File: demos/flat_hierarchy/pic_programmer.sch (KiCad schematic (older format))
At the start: 50 parts, among them J1 DB9-FEMAL, P1 CONN_2, Q1 BC237, Q2 BC307, Q3 BC307, U2 74HC125, U3 7805, U4 LT1373

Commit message: Update demo files
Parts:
- D12: Champ4 (none) -> YELLOW-LED
- D8: Champ4 (none) -> Low Current Led; Champ5 (none) -> RED LED
- D9: Champ4 (none) -> GREEN LED
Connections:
- net VPP/MCLR renamed VPP-MCLR

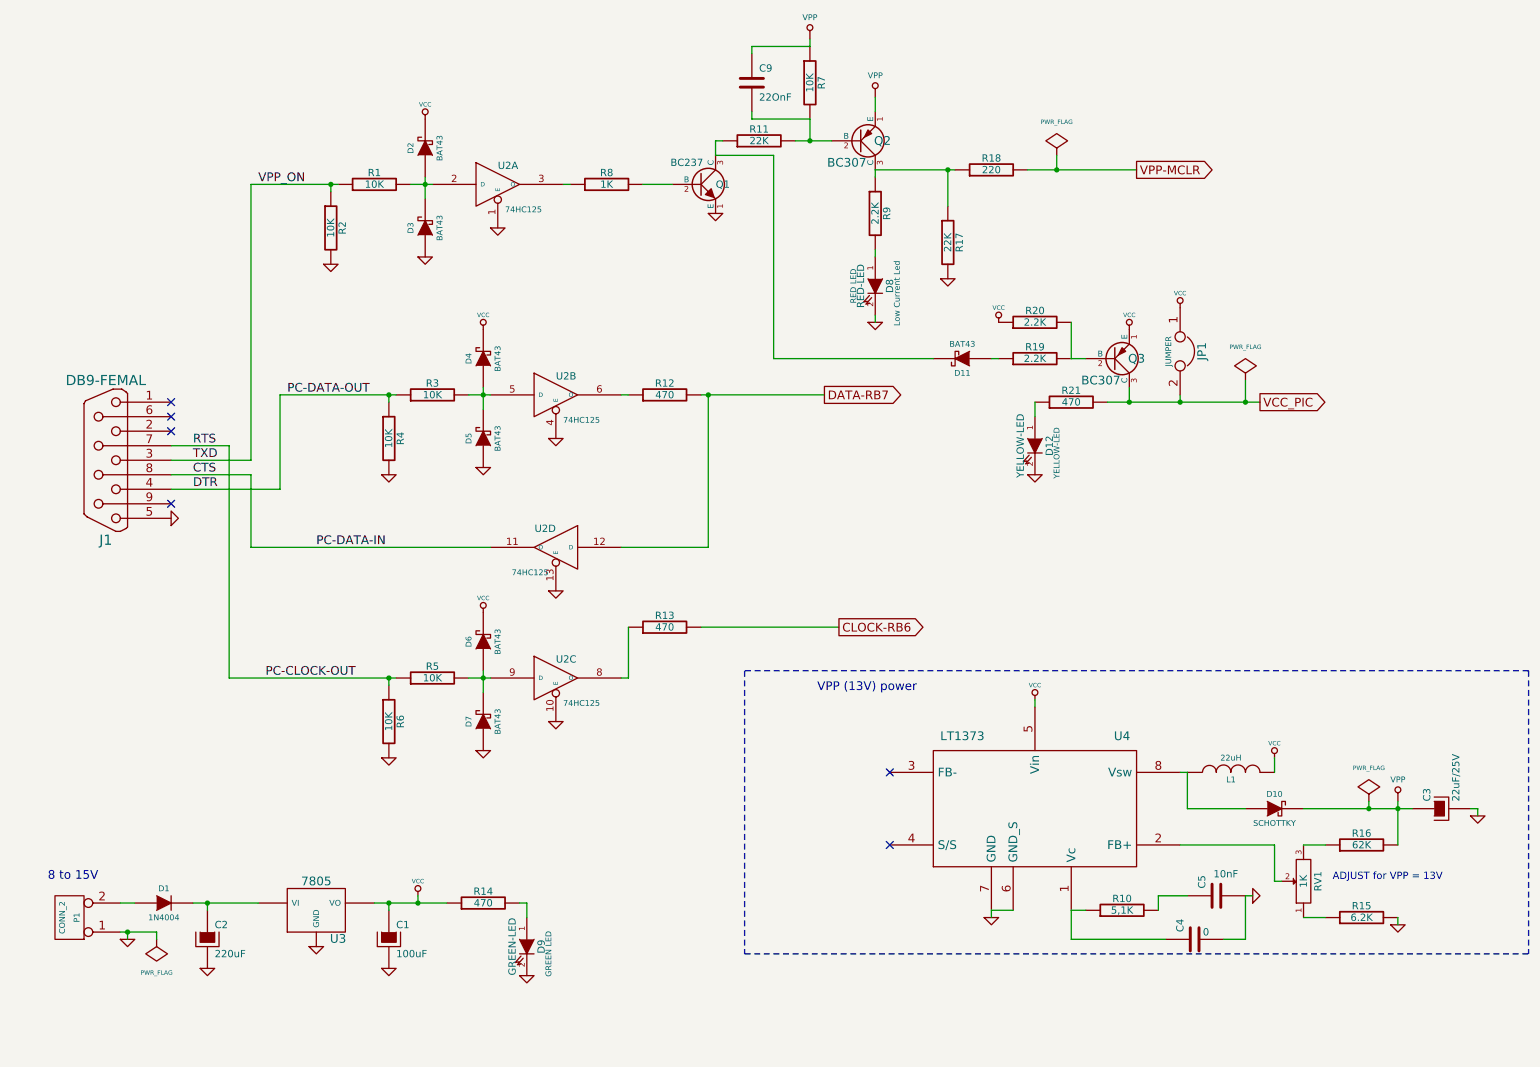
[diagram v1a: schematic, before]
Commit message: demos/ schematic tidying
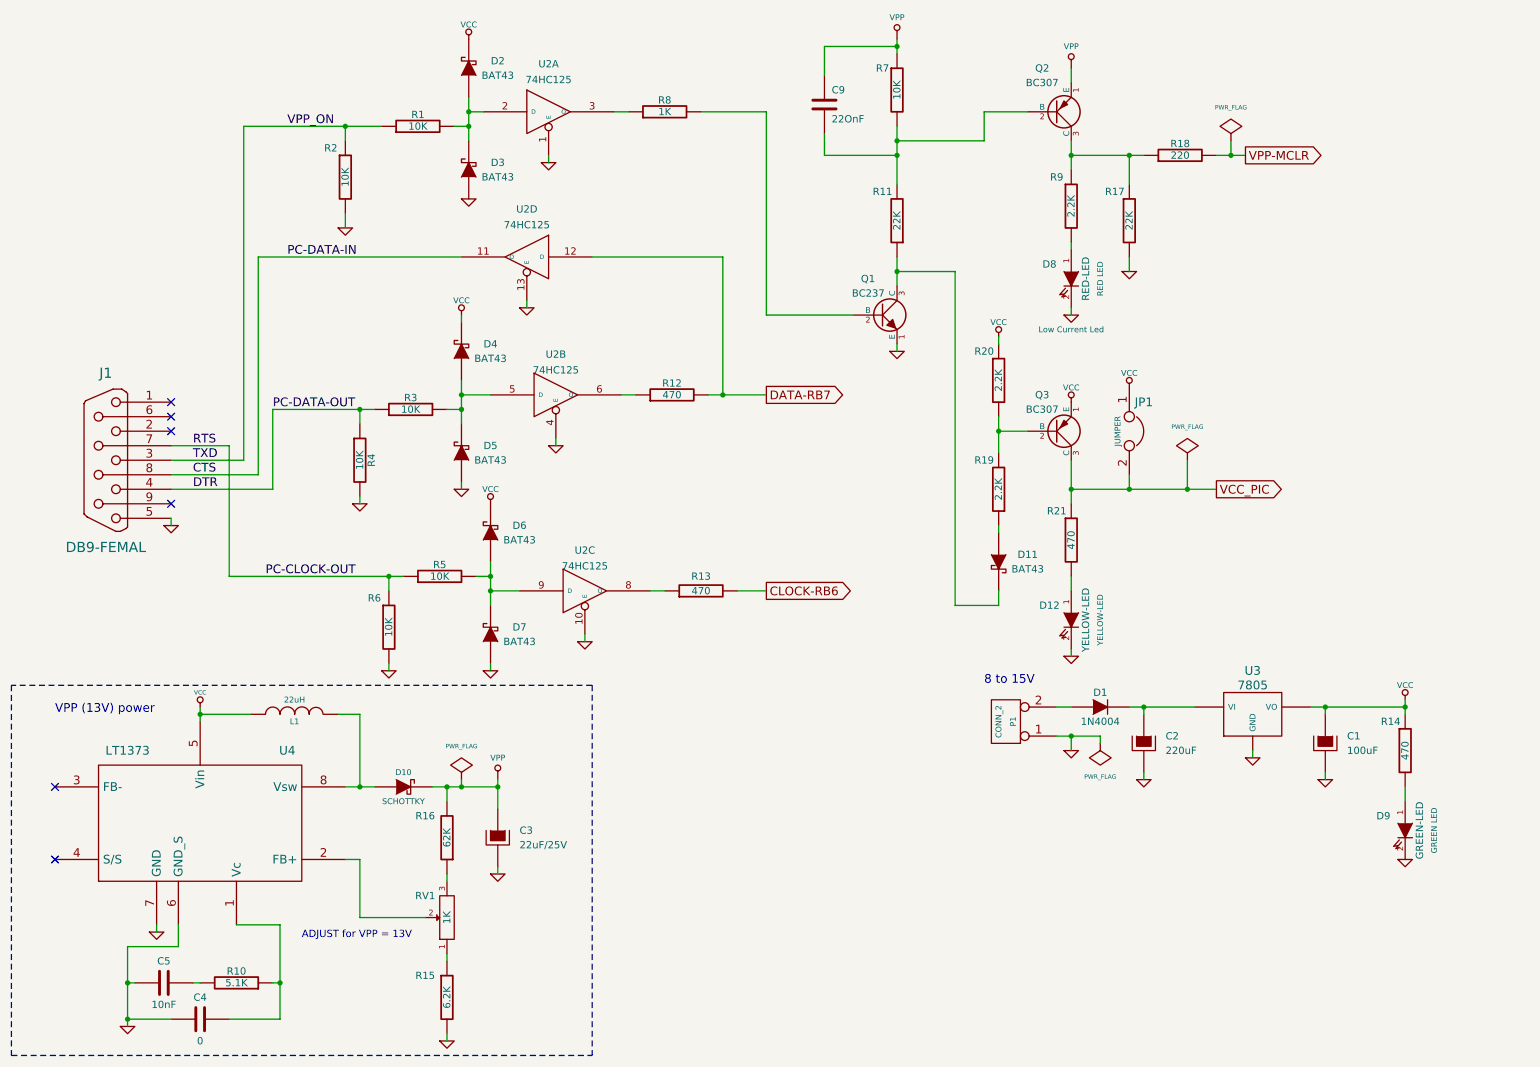
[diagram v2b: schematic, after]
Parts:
- R10: value 5,1K -> 5.1K
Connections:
- net VCC_PIC: now also R21.1; no longer R21.2
- net at D12.1 (A): now also R21.2; no longer R21.1
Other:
- moved on the sheet: C1, C2, C3, C4, C5, C9, D1, D10, D11, D12, D2, D3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

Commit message: polygons in footprint body: fix incorrect calculation of polygons with clearance or outline thickness (fix bug #1511366) Clean demos
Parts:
- C1, C2: footprint (none) -> Discret:CP10
- C3: footprint (none) -> Discret:CP8
- C4, C5, C9: footprint (none) -> Discret:C1-1
- D1, D10: footprint (none) -> Discret:D5
- D11, D2, D3, D4, D5, D6, D7: footprint (none) -> Discret:D3
- D12, D8, D9: footprint (none) -> Discret:LEDV
- J1: footprint (none) -> Connect:DB9FC
- JP1: footprint (none) -> pin_array:PIN_ARRAY_2X1
- L1: footprint (none) -> inductors:INDUCTOR_V
- P1: footprint (none) -> Connect:bornier2
- Q1, Q2, Q3: footprint (none) -> Discret:TO92
- R1, R10, R11, R12, R13, R14, R15, R16, R17, R18, R19, R2, R20, R21, R3, R4, R5, R6, R7, R8, R9: footprint (none) -> Discret:R4
- RV1: footprint (none) -> Discret:RV2X4
- U2: footprint (none) -> Sockets_DIP:DIP-10__300_ELL
- U3: footprint (none) -> Discret:LM78XX
- U4: footprint (none) -> Sockets_DIP:DIP-8__300_ELL
